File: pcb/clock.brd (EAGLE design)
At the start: 145 x 50 mm, 71 parts, among them IC1 STM32F072C8T6, IC2 REG1117, IC3 24C64ST, X3 USB-MICROB

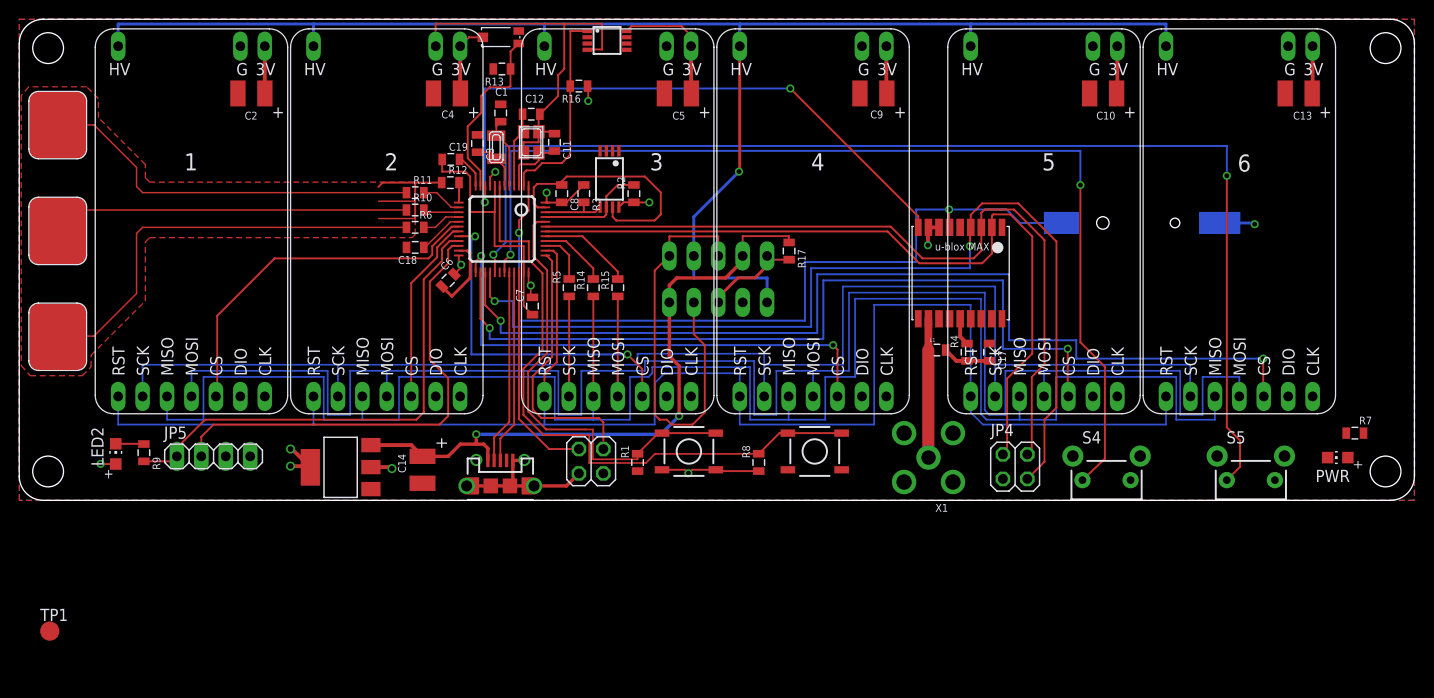
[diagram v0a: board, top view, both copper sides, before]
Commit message: added silkscreen labels
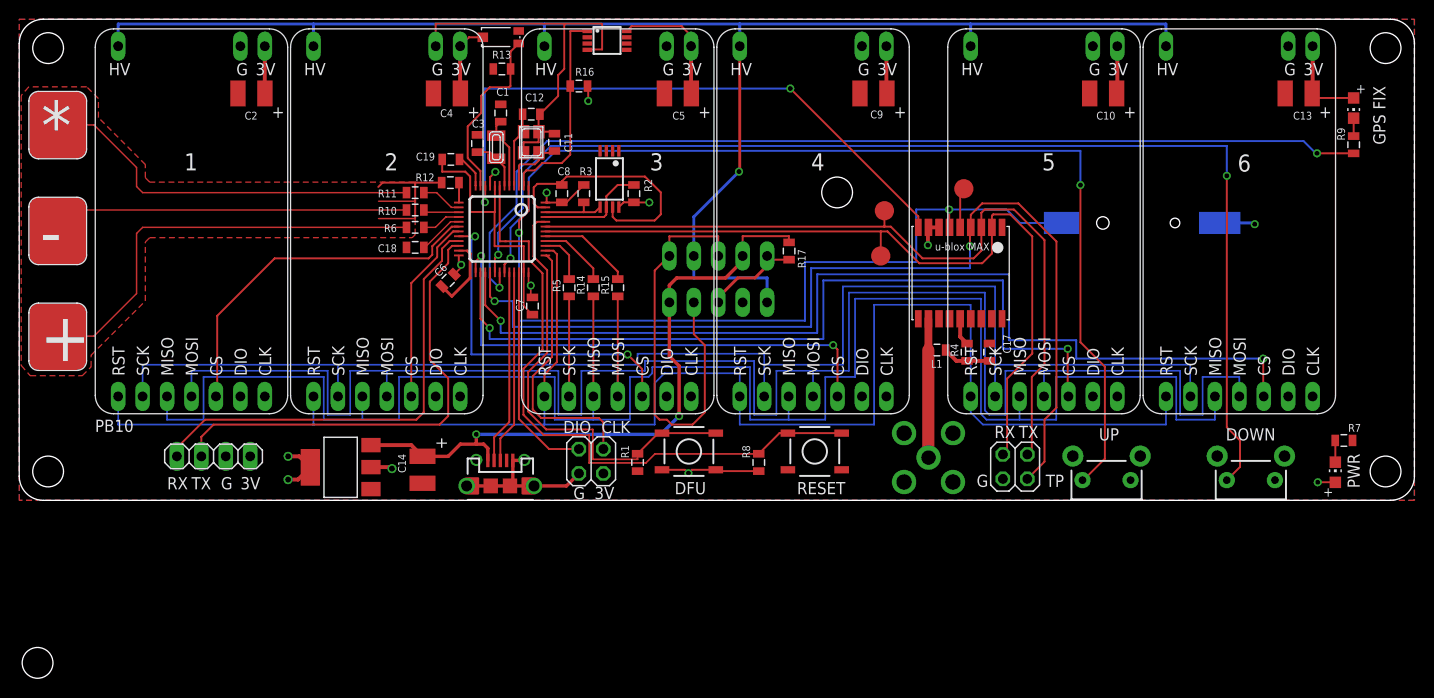
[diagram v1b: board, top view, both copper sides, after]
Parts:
- added TP2, TP3: PTR1TP20R, testpad:TP20R
- added U$20, U$21: M3_MOUNTING_HOLE, a:M3_MOUNTING_HOLE_PACK
- moved LED2 133.6 mm to (138.7, 40.8), turned to 180 degrees
- moved R9 129.7 mm to (138.7, 37.0), turned to 270 degrees
- moved TP1 105.5 mm to (98.2, 32.4)
- moved PWR 1.55 mm to (136.8, 2.92), turned to 0 degrees
- moved R7 1.37 mm to (137.7, 6.22)
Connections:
- new net N$24: IC1.30, R9.2
- new net N$25: TP1.TP, U$7.5_EXTINT
- net N$21: now also R9.1; no longer R9.2
- net RX3: no longer R9.1
- net USART1_RX: now also TP3.TP
- net USART1_TX: now also TP2.TP
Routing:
- net N$24: track 0.00 -> 104.1 mm, vias 0 -> 2
- net +3V3: track 80.3 -> 85.9 mm
- net N$25: track 0.00 -> 4.17 mm
- net RX3: track 51.6 -> 48.7 mm
- net N$23: track 124.5 -> 121.7 mm
- net N$22: track 108.4 -> 105.7 mm
- net USART1_TX: track 81.9 -> 84.5 mm
- net N$27: track 0.00 -> 2.26 mm
- net USART1_RX: track 82.0 -> 83.6 mm
- net N$21: track 2.93 -> 1.86 mm
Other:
- board text added: "*"
- board text added: "+"
- board text added: "-"
- board text added: "3V"
- board text added: "CLK"
- board text added: "DFU"
- board text added: "DIO"
- board text added: "DOWN"
- board text added: "G"
- board text added: "GPS FIX"
- board text added: "PB10"
- board text added: "RESET"
- board text added: "RX"
- board text added: "TP"
- board text added: "TX"
- board text added: "UP"

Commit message: drunk
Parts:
- removed U$21: M3_MOUNTING_HOLE, a:M3_MOUNTING_HOLE_PACK
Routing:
- net GPS_RESET: track 65.2 -> 71.8 mm
- net TX3: track 49.6 -> 48.3 mm
- net RX3: track 48.7 -> 47.9 mm
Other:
- board text added: "exixe clock dekuNukem 2017"
- board text removed: "PB10"
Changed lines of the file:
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@@
 <layer number="14" name="Route14" color="1" fill="6" visible="no" active="no"/>
 <layer number="15" name="Route15" color="4" fill="6" visible="no" active="yes"/>
-<layer number="16" name="Bottom" color="1" fill="1" visible="yes" active="yes"/>
+<layer number="16" name="Bottom" color="1" fill="1" visible="no" active="yes"/>
 <layer number="17" name="Pads" color="2" fill="1" visible="yes" active="yes"/>
 <layer number="18" name="Vias" color="2" fill="1" visible="yes" active="yes"/>
@@
 <text x="20.955" y="1.143" size="1.27" layer="25">G</text>
 <text x="22.987" y="1.143" size="1.27" layer="25">3V</text>
-<text x="7.874" y="7.112" size="1.27" layer="25">PB10</text>
 <text x="61.849" y="1.397" size="1.27" layer="25" rot="R180">3V</text>
 <text x="58.801" y="1.397" size="1.27" layer="25" rot="R180">G</text>
@@
 <text x="130.556" y="7.493" size="1.27" layer="25" rot="R180">DOWN</text>
 <text x="2.159" y="14.478" size="5.08" layer="25">+</text>
-<text x="2.159" y="25.4" size="5.08" layer="25">-</text>
-<text x="2.286" y="36.449" size="5.08" layer="25">*</text>
+<text x="2.286" y="36.449" size="5.08" layer="25">-</text>
+<text x="2.286" y="25.4" size="5.08" layer="25">*</text>
 <text x="140.716" y="43.053" size="1.27" layer="25" rot="R270">GPS FIX</text>
+<text x="139.573" y="26.67" size="1.27" layer="25" rot="R270">exixe clock
+dekuNukem 2017</text>
 </plain>
 <attributes>
@@
 <element name="R9" library="clock" package="0805" value="" x="138.684" y="36.957" rot="R270"/>
 <element name="U$20" library="a" package="M3_MOUNTING_HOLE_PACK" value="M3_MOUNTING_HOLE" x="85" y="32"/>
-<element name="U$21" library="a" package="M3_MOUNTING_HOLE_PACK" value="M3_MOUNTING_HOLE" x="1.905" y="-16.891"/>
 <element name="TP2" library="testpad" library_urn="urn:adsk.eagle:library:385" package="TP20R" value="PTR1TP20R" x="89.535" y="25.4" smashed="yes">
 <attribute name="TP_SIGNAL_NAME" value="" x="89.535" y="22.86" size="1" layer="37"/>
@@
 <wire x1="53.975" y1="39.994" x2="53.975" y2="38.311" width="0.2032" layer="1"/>
 <wire x1="67.564" y1="25.4" x2="66.04" y2="23.876" width="0.2032" layer="1"/>
-<wire x1="66.04" y1="23.876" x2="66.04" y2="8.89" width="0.2032" layer="1"/>
-<wire x1="66.04" y1="8.89" x2="66.548" y2="8.382" width="0.2032" layer="1"/>
+<wire x1="66.04" y1="8.89" x2="66.04" y2="23.876" width="0.3556" layer="1"/>
+<wire x1="66.548" y1="8.382" x2="66.04" y2="8.89" width="0.2032" layer="1"/>
 <wire x1="66.548" y1="8.382" x2="67.31" y2="8.382" width="0.2032" layer="1"/>
 <wire x1="67.31" y1="8.382" x2="67.818" y2="7.874" width="0.2032" layer="1"/>
@@
 <wire x1="43.942" y1="26.162" x2="43.942" y2="24.892" width="0.2032" layer="1"/>
 <wire x1="42.037" y1="22.987" x2="43.942" y2="24.892" width="0.2032" layer="1"/>
-<wire x1="41.275" y1="8.382" x2="19.304" y2="8.382" width="0.2032" layer="1"/>
 <wire x1="41.275" y1="8.382" x2="42.037" y2="9.144" width="0.2032" layer="1"/>
 <wire x1="42.037" y1="9.144" x2="42.037" y2="22.987" width="0.2032" layer="1"/>
-<wire x1="19.304" y1="8.382" x2="16.383" y2="5.461" width="0.2032" layer="1"/>
-<wire x1="16.383" y1="5.461" x2="16.383" y2="4.572" width="0.2032" layer="1"/>
-<wire x1="16.383" y1="4.572" x2="15.864" y2="4.053" width="0.2032" layer="1"/>
+<wire x1="16.383" y1="4.572" x2="16.383" y2="5.461" width="0.2032" layer="1"/>
+<wire x1="16.383" y1="5.461" x2="18.288" y2="7.366" width="0.2032" layer="1"/>
+<wire x1="18.288" y1="7.366" x2="29.972" y2="7.366" width="0.2032" layer="1"/>
+<wire x1="29.972" y1="7.366" x2="30.988" y2="8.382" width="0.2032" layer="1"/>
+<wire x1="30.988" y1="8.382" x2="41.275" y2="8.382" width="0.2032" layer="1"/>
 </signal>
 <signal name="TX3">
@@
 <wire x1="42.672" y1="22.733" x2="42.672" y2="14.605" width="0.2032" layer="1"/>
 <wire x1="42.672" y1="14.605" x2="44.577" y2="12.7" width="0.2032" layer="1"/>
-<wire x1="43.688" y1="7.874" x2="20.193" y2="7.874" width="0.2032" layer="1"/>
 <wire x1="44.577" y1="12.7" x2="44.577" y2="8.763" width="0.2032" layer="1"/>
-<wire x1="44.577" y1="8.763" x2="43.688" y2="7.874" width="0.2032" layer="1"/>
-<wire x1="20.193" y1="7.874" x2="18.923" y2="6.604" width="0.2032" layer="1"/>
-<wire x1="18.923" y1="6.604" x2="18.923" y2="4.572" width="0.2032" layer="1"/>
-<wire x1="18.923" y1="4.572" x2="18.923" y2="3.672" width="0.2032" layer="1"/>
+<wire x1="43.688" y1="7.874" x2="44.577" y2="8.763" width="0.2032" layer="1"/>
+<wire x1="18.923" y1="4.572" x2="18.923" y2="5.969" width="0.2032" layer="1"/>
+<wire x1="18.923" y1="5.969" x2="19.685" y2="6.731" width="0.2032" layer="1"/>
+<wire x1="19.685" y1="6.731" x2="30.226" y2="6.731" width="0.2032" layer="1"/>
+<wire x1="30.226" y1="6.731" x2="31.369" y2="7.874" width="0.2032" layer="1"/>
+<wire x1="31.369" y1="7.874" x2="43.688" y2="7.874" width="0.2032" layer="1"/>
 </signal>
 <signal name="DS18B20_DATA">
@@
 <via x="80.137" y="42.799" extent="1-16" drill="0.5"/>
 <wire x1="48.387" y1="30.988" x2="48.387" y2="42.799" width="0.2032" layer="16"/>
-<wire x1="93.4392" y1="28.3688" x2="93.4392" y2="29.4968" width="0.2032" layer="1"/>
-<wire x1="93.4392" y1="29.4968" x2="80.137" y2="42.799" width="0.2032" layer="1"/>
+<wire x1="80.137" y1="42.799" x2="80.137" y2="37.973" width="0.2032" layer="1"/>
+<wire x1="80.137" y1="37.973" x2="81.28" y2="36.83" width="0.2032" layer="1"/>
+<wire x1="81.28" y1="36.83" x2="92.456" y2="36.83" width="0.2032" layer="1"/>
+<wire x1="92.456" y1="36.83" x2="93.4392" y2="35.8468" width="0.2032" layer="1"/>
+<wire x1="93.4392" y1="35.8468" x2="93.4392" y2="28.3688" width="0.2032" layer="1"/>
 </signal>
 <signal name="N$22">
@@
 <contactref element="S4" pad="1"/>
 <via x="51.054" y="25.146" extent="1-16" drill="0.5"/>
-<wire x1="110.2868" y1="36.322" x2="110.2868" y2="32.766" width="0.2032" layer="16"/>
-<via x="110.2868" y="32.766" extent="1-16" drill="0.5"/>
+<wire x1="110.2868" y1="36.322" x2="110.2868" y2="33.782" width="0.2032" layer="16"/>
+<via x="110.2868" y="33.782" extent="1-16" drill="0.5"/>
 <wire x1="55.753" y1="36.322" x2="110.2868" y2="36.322" width="0.2032" layer="16"/>
-<wire x1="110.2868" y1="32.766" x2="110.2868" y2="16.4338" width="0.2032" layer="1"/>
+<wire x1="110.2868" y1="33.782" x2="110.2868" y2="16.4338" width="0.2032" layer="1"/>
 <wire x1="110.2868" y1="16.4338" x2="112.8268" y2="13.8938" width="0.2032" layer="1"/>
 <wire x1="112.8268" y1="13.8938" x2="112.8268" y2="4.3268" width="0.2032" layer="1"/>
@@
 <via x="49.784" y="25.527" extent="1-16" drill="0.5"/>
 <wire x1="55.245" y1="36.83" x2="125.5014" y2="36.83" width="0.2032" layer="16"/>
-<wire x1="125.5014" y1="36.83" x2="125.5014" y2="33.7312" width="0.2032" layer="16"/>
-<via x="125.5014" y="33.7312" extent="1-16" drill="0.5"/>
-<wire x1="125.5014" y1="33.7312" x2="125.5014" y2="7.5946" width="0.2032" layer="1"/>
+<wire x1="125.5014" y1="36.83" x2="125.5014" y2="33.782" width="0.2032" layer="16"/>
+<via x="125.5014" y="33.782" extent="1-16" drill="0.5"/>
+<wire x1="125.5014" y1="33.782" x2="125.5014" y2="7.5946" width="0.2032" layer="1"/>
 <wire x1="125.5014" y1="7.5946" x2="126.873" y2="6.223" width="0.2032" layer="1"/>
 <wire x1="126.873" y1="6.223" x2="126.873" y2="3.473" width="0.2032" layer="1"/>
@@
 </drawing>
 <compatibility>
+<note version="6.3" minversion="6.2.2" severity="warning">
+Since Version 6.2.2 text objects can contain more than one line,
+which will not be processed correctly with this version.
+</note>
 <note version="8.2" severity="warning">
 Since Version 8.2, Eagle supports online libraries. The ids

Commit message: final
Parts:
- moved TP3 10.3 mm to (79.6, 30.4)
- moved TP2 5.73 mm to (83.8, 25.8)
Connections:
- net RX3 renamed PB10
- net TX3 renamed PB11
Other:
- board text added: "EXTINT"
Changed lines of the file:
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@@
 <rectangle x1="74.2188" y1="33.5788" x2="75.4888" y2="45.2628" layer="41"/>
 <rectangle x1="73.025" y1="44.704" x2="76.708" y2="50.038" layer="42"/>
-<text x="15.367" y="1.143" size="1.27" layer="25">RX</text>
-<text x="17.907" y="1.143" size="1.27" layer="25">TX</text>
+<text x="15.367" y="1.143" size="1.27" layer="25">TX</text>
+<text x="17.907" y="1.143" size="1.27" layer="25">RX</text>
 <text x="20.955" y="1.143" size="1.27" layer="25">G</text>
 <text x="22.987" y="1.143" size="1.27" layer="25">3V</text>
@@
 <text x="2.286" y="36.449" size="5.08" layer="25">-</text>
 <text x="2.286" y="25.4" size="5.08" layer="25">*</text>
-<text x="140.716" y="43.053" size="1.27" layer="25" rot="R270">GPS FIX</text>
+<text x="139.954" y="42.672" size="1.27" layer="25" rot="R270">GPS
+FIX</text>
 <text x="139.573" y="26.67" size="1.27" layer="25" rot="R270">exixe clock
 dekuNukem 2017</text>
+<text x="78.74" y="32.004" size="1.27" layer="25">RX</text>
+<text x="82.677" y="22.86" size="1.27" layer="25">TX</text>
+<text x="99.695" y="31.75" size="1.27" layer="25">EXTINT</text>
 </plain>
 <attributes>
@@
 <element name="R9" library="clock" package="0805" value="" x="138.684" y="36.957" rot="R270"/>
 <element name="U$20" library="a" package="M3_MOUNTING_HOLE_PACK" value="M3_MOUNTING_HOLE" x="85" y="32"/>
-<element name="TP2" library="testpad" library_urn="urn:adsk.eagle:library:385" package="TP20R" value="PTR1TP20R" x="89.535" y="25.4" smashed="yes">
-<attribute name="TP_SIGNAL_NAME" value="" x="89.535" y="22.86" size="1" layer="37"/>
-<attribute name="VALUE" x="88.773" y="24.384" size="0.0254" layer="27"/>
-</element>
-<element name="TP3" library="testpad" library_urn="urn:adsk.eagle:library:385" package="TP20R" value="PTR1TP20R" x="89.916" y="30.099" smashed="yes">
-<attribute name="TP_SIGNAL_NAME" value="" x="89.916" y="27.559" size="1" layer="37"/>
-<attribute name="VALUE" x="89.154" y="29.083" size="0.0254" layer="27"/>
+<element name="TP2" library="testpad" library_urn="urn:adsk.eagle:library:385" package="TP20R" value="PTR1TP20R" x="83.82" y="25.781" smashed="yes">
+<attribute name="TP_SIGNAL_NAME" value="" x="83.82" y="23.241" size="1" layer="37"/>
+<attribute name="VALUE" x="83.058" y="24.765" size="0.0254" layer="27"/>
+</element>
+<element name="TP3" library="testpad" library_urn="urn:adsk.eagle:library:385" package="TP20R" value="PTR1TP20R" x="79.629" y="30.353" smashed="yes">
+<attribute name="TP_SIGNAL_NAME" value="" x="79.629" y="27.813" size="1" layer="37"/>
+<attribute name="VALUE" x="78.867" y="29.337" size="0.0254" layer="27"/>
 </element>
 </elements>
@@
 <contactref element="IC1" pad="42"/>
 <contactref element="U$7" pad="2_TXD"/>
-<wire x1="89.535" y1="27.948" x2="54.682" y2="27.948" width="0.2032" layer="1"/>
-<wire x1="89.535" y1="27.948" x2="90.2382" y2="27.948" width="0.2032" layer="1"/>
+<wire x1="83.693" y1="27.948" x2="90.2382" y2="27.948" width="0.2032" layer="1"/>
+<wire x1="83.693" y1="27.948" x2="54.682" y2="27.948" width="0.2032" layer="1"/>
 <wire x1="93.5482" y1="24.638" x2="100.076" y2="24.638" width="0.2032" layer="1"/>
 <wire x1="101.0892" y1="25.6512" x2="100.076" y2="24.638" width="0.2032" layer="1"/>
@@
 <wire x1="105.283" y1="27.432" x2="105.283" y2="15.2654" width="0.2032" layer="1"/>
 <contactref element="TP2" pad="TP"/>
-<wire x1="89.535" y1="25.4" x2="89.535" y2="27.948" width="0.2032" layer="1"/>
+<wire x1="83.82" y1="25.781" x2="83.82" y2="27.948" width="0.2032" layer="1"/>
+<wire x1="83.82" y1="27.948" x2="83.693" y2="27.948" width="0.2032" layer="1"/>
 </signal>
 <signal name="USART1_RX">
 <contactref element="IC1" pad="43"/>
 <contactref element="U$7" pad="3_RXD"/>
-<wire x1="89.916" y1="28.448" x2="54.682" y2="28.448" width="0.2032" layer="1"/>
-<wire x1="89.916" y1="28.448" x2="90.5764" y2="28.448" width="0.2032" layer="1"/>
+<wire x1="79.629" y1="28.448" x2="90.5764" y2="28.448" width="0.2032" layer="1"/>
+<wire x1="79.629" y1="28.448" x2="54.682" y2="28.448" width="0.2032" layer="1"/>
 <wire x1="90.5764" y1="28.448" x2="93.8784" y2="25.146" width="0.2032" layer="1"/>
 <wire x1="99.9998" y1="28.3582" x2="99.9892" y2="28.3688" width="0.2032" layer="1"/>
@@
 <wire x1="106.553" y1="27.051" x2="106.553" y2="14.1478" width="0.2032" layer="1"/>
 <contactref element="TP3" pad="TP"/>
-<wire x1="89.916" y1="30.099" x2="89.916" y2="28.448" width="0.2032" layer="1"/>
+<wire x1="79.629" y1="30.353" x2="79.629" y2="28.448" width="0.2032" layer="1"/>
 </signal>
 <signal name="N$9">
@@
 <wire x1="106.553" y1="4.013" x2="104.77" y2="2.23" width="0.2032" layer="1"/>
 </signal>
-<signal name="RX3">
+<signal name="PB10">
 <contactref element="JP5" pad="1"/>
 <contactref element="IC1" pad="21"/>
@@
 <wire x1="30.988" y1="8.382" x2="41.275" y2="8.382" width="0.2032" layer="1"/>
 </signal>
-<signal name="TX3">
+<signal name="PB11">
 <contactref element="JP5" pad="2"/>
 <contactref element="IC1" pad="22"/>
